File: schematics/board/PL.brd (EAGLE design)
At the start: 89 x 89 mm, 25 parts, among them IC2 STM32F103C8T, Q5 8MHz

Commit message: Исправлена плата TESTPL
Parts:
- added R1, R2, R3: 10k, resistor:R0603
- moved PWR 121.4 mm to (65.4, 41.8), turned to 180 degrees
- moved R102 112.5 mm to (54.7, 27.0), turned to 90 degrees
- moved R64 108.5 mm to (56.8, 49.5), turned to 270 degrees
- moved R79 107.7 mm to (43.0, 35.4), turned to 180 degrees
- moved C48 105.5 mm to (63.3, 40.2), turned to 270 degrees
- moved R101 104.4 mm to (52.6, 27.0), turned to 90 degrees
- moved U$23 102.3 mm to (55.5, 5.00)
- moved R27 101.3 mm to (54.6, 49.6), turned to 270 degrees
- moved C005R 97.1 mm to (46.0, 38.6)
- moved PB5 95.6 mm to (67.6, 41.8), turned to 180 degrees
- moved C44 92.6 mm to (26.5, 24.6), turned to 270 degrees
- moved R26 92.1 mm to (50.4, 49.5), turned to 270 degrees
- moved R82 92.1 mm to (65.4, 38.4), turned to 90 degrees
- moved MICS-6814 91.9 mm to (65.3, 67.7), turned to 180 degrees
- moved BME280 90.5 mm to (50.0, 69.0), turned to 180 degrees
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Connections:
- removed net VBAT: IC2.1
- new net SENS_CO: IC2.10, MICS-6814.P$5, R3.1
- new net SENS_NH3: IC2.11, MICS-6814.P$4, R2.1
- new net SENS_NO2: IC2.12, MICS-6814.P$3, R1.1
- new net SENS_O2: IC2.13, ME-O2.P$1
- net SCL: now also BME280.P$3
- net SDA: now also BME280.P$4
- net VDD: now also IC2.1, R1.2, R2.2, R3.2
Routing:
- net VDD: track 0.00 -> 140.4 mm, vias 0 -> 3
- net 5V: track 0.00 -> 109.7 mm
- net N$145: track 0.00 -> 6.50 mm
- net N$133: track 0.00 -> 6.41 mm
- net SENS_CO: track 0.00 -> 3.12 mm
- net SENS_NO2: track 0.00 -> 3.12 mm
- net SENS_NH3: track 0.00 -> 3.01 mm
- net N$159: track 0.00 -> 1.80 mm
- net N$1: track 0.00 -> 1.73 mm
- added copper zone on layer 1, net GND
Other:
- outline, holes or cut-outs redrawn

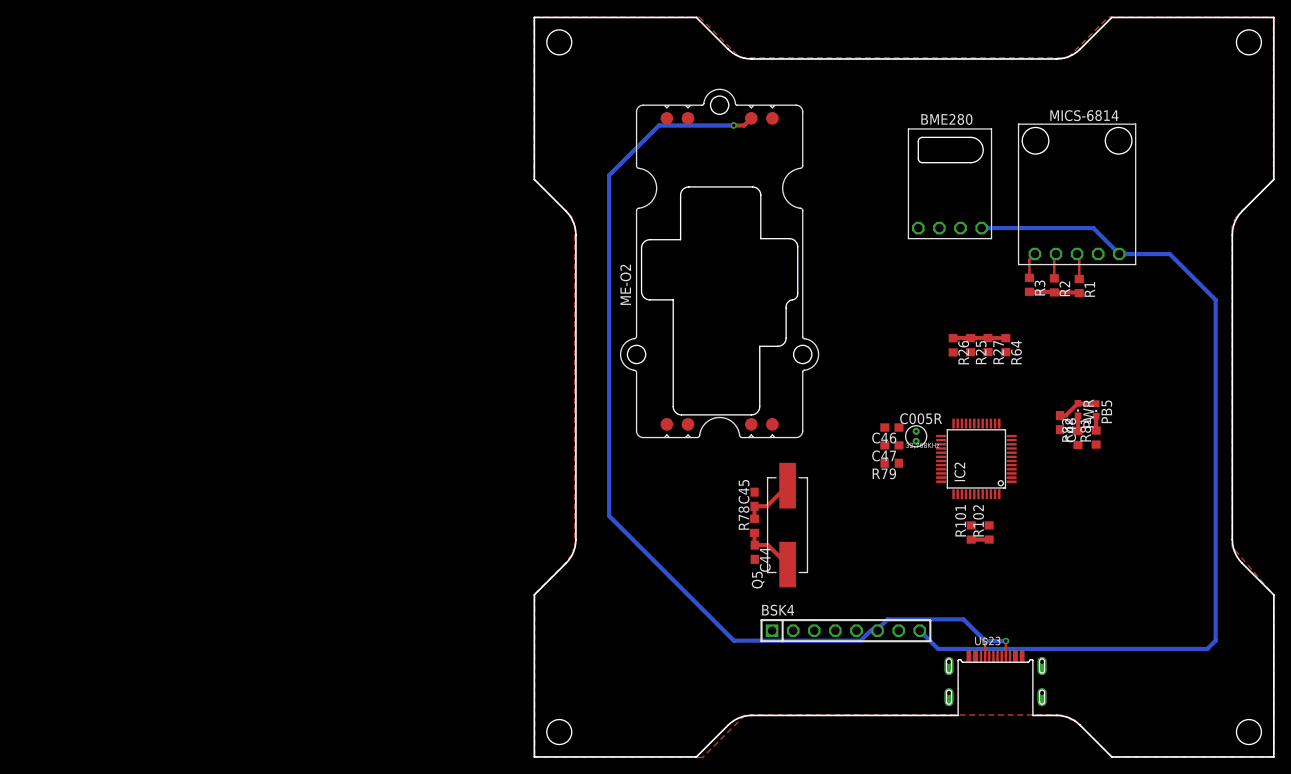
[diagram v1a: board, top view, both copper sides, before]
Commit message: Разведена плата PL
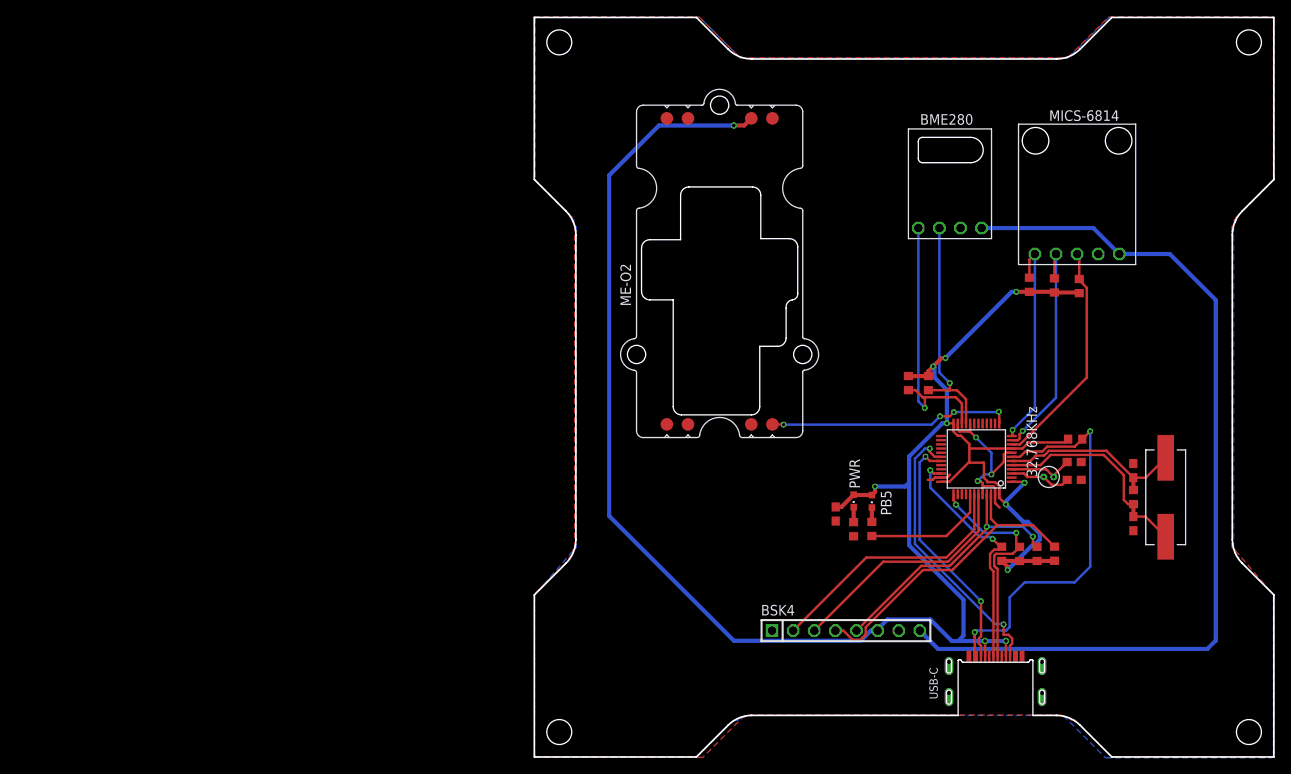
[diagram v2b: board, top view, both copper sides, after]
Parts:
- moved C44 46.6 mm to (72.1, 34.5), turned to 90 degrees
- moved R78 45.7 mm to (72.1, 31.3), turned to 270 degrees
- moved C45 45.7 mm to (72.1, 28.1), turned to 270 degrees
- moved Q5 45.6 mm to (76.0, 31.2), turned to 270 degrees
- moved PB5 29.2 mm to (40.6, 30.8)
- moved PWR 29.2 mm to (38.4, 30.8)
- moved R81 29.2 mm to (40.6, 27.4)
- moved C48 29.2 mm to (36.3, 29.2)
- moved R82 29.2 mm to (38.4, 27.4)
- moved R26 27.9 mm to (62.6, 24.5), turned to 90 degrees
- moved R25 26.4 mm to (60.5, 24.4), turned to 90 degrees
- moved R27 25.4 mm to (58.4, 24.4), turned to 90 degrees
- moved R64 25.1 mm to (56.2, 24.4), turned to 90 degrees
- moved C46 22.8 mm to (65.0, 33.4), turned to 0 degrees
- moved R79 22.3 mm to (65.1, 38.2), turned to 0 degrees
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- renumbered U$23 to USB-C
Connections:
- net SENS_CO: now also IC2.12; no longer IC2.10
- net SENS_NO2: now also IC2.10; no longer IC2.12
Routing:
- net VDD: track 140.4 -> 251.6 mm, vias 3 -> 11
- net NRST: track 0.00 -> 49.2 mm, vias 0 -> 2
- net SDATM: track 0.00 -> 38.2 mm
- net TX-C: track 0.00 -> 34.0 mm, vias 0 -> 2
- net SDA: track 0.00 -> 32.8 mm, vias 0 -> 1
- net SCLTM: track 0.00 -> 32.4 mm, vias 0 -> 2
- net TIME: track 0.00 -> 31.1 mm
- net RX-C: track 0.00 -> 29.7 mm, vias 0 -> 2
- net SWD: track 0.00 -> 29.4 mm, vias 0 -> 2
- net SENS_O2: track 0.00 -> 29.4 mm, vias 0 -> 4
- net I2CINT: track 0.00 -> 29.2 mm
- net SCL: track 0.00 -> 27.9 mm, vias 0 -> 1
- net SWC: track 0.00 -> 27.7 mm, vias 0 -> 2
- net SENS_NH3: track 3.01 -> 28.1 mm, vias 0 -> 1
- net GND: track 0.00 -> 24.9 mm, vias 0 -> 3
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- added copper zone on layer 16, net GND

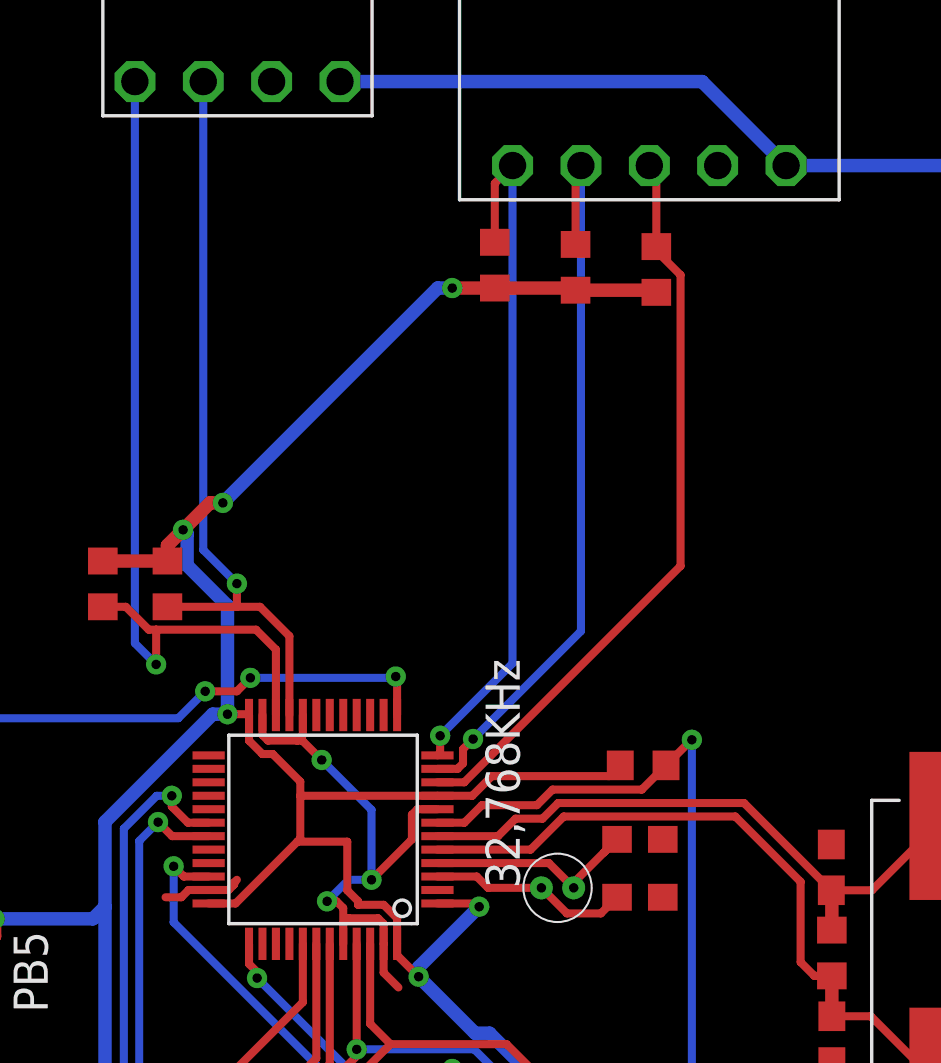
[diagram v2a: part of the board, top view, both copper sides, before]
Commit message: На плату полезной нагрузки добавлены управляемые резисторы для управления балансирующими сопротивлениями для газового датчика
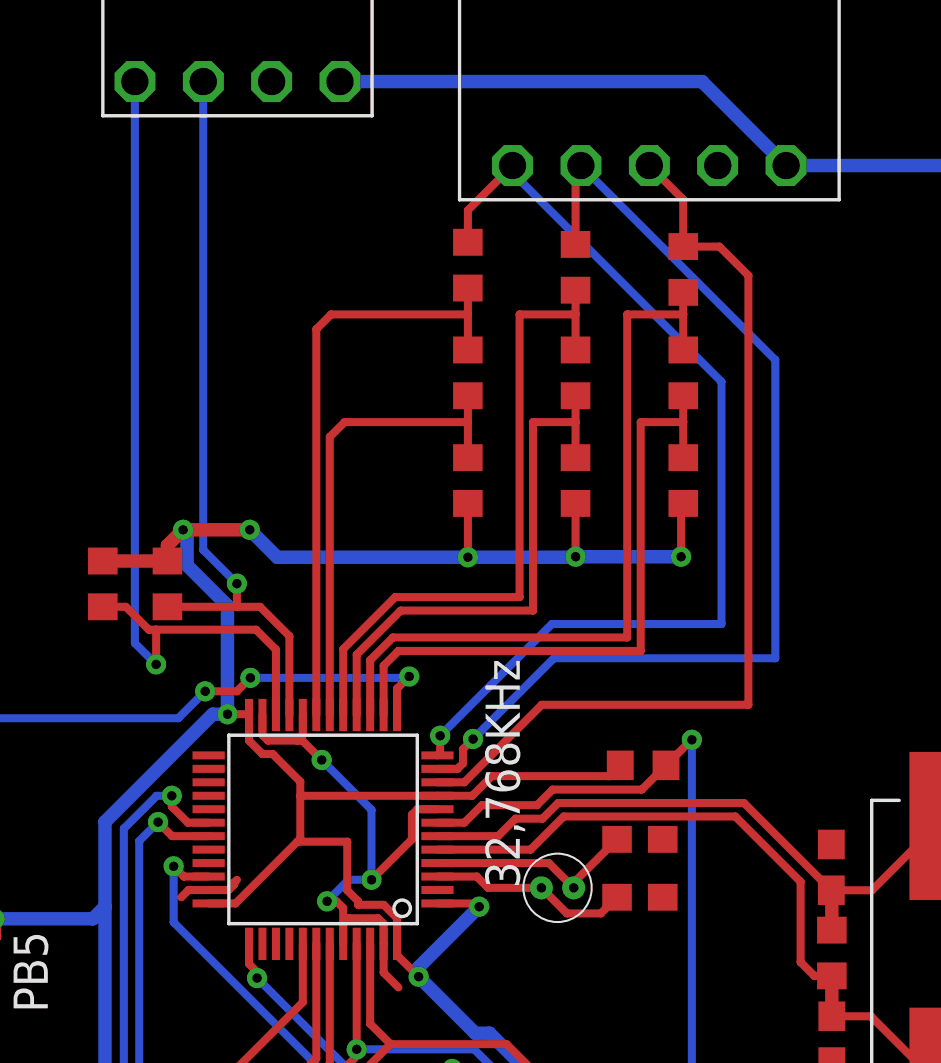
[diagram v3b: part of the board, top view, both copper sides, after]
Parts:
- added R4, R5, R6, R7, R8, R9: 10k, resistor:R0603
- moved R1 1.00 mm to (66.6, 56.7)
- moved R3 1.00 mm to (58.6, 56.8)
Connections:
- new net SENS_CTL_CO_1: IC2.19, R3.2, R6.1
- new net SENS_CTL_CO_2: IC2.18, R6.2, R7.1
- new net SENS_CTL_NH3_1: IC2.17, R2.2, R5.1
- new net SENS_CTL_NH3_2: IC2.16, R5.2, R8.1
- new net SENS_CTL_NO2_1: IC2.15, R1.2, R4.1
- new net SENS_CTL_NO2_2: IC2.14, R4.2, R9.1
- net VDD: now also R7.2, R8.2, R9.2; no longer R1.2, R2.2, R3.2
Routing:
- net SENS_CTL_NO2_1: track 0.00 -> 28.2 mm
- net SENS_CTL_NH3_1: track 0.00 -> 24.6 mm
- net SENS_CTL_NO2_2: track 0.00 -> 24.0 mm
- net SENS_CTL_CO_1: track 0.00 -> 22.5 mm
- net SENS_CTL_NH3_2: track 0.00 -> 20.4 mm
- net SENS_CTL_CO_2: track 0.00 -> 18.0 mm
- net SENS_NH3: track 28.1 -> 38.9 mm
- net SENS_CO: track 26.2 -> 36.7 mm
- net SENS_NO2: track 27.7 -> 35.1 mm
- net VDD: track 251.6 -> 255.2 mm, vias 11 -> 13
- net N$148: track 8.60 -> 7.91 mm
- net SENS_O2: track 29.4 -> 30.0 mm
- net GND: track 24.9 -> 24.3 mm

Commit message: Доработана плата БКУ
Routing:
- net SENS_NH3: track 38.9 -> 36.7 mm
- net SENS_NO2: track 35.1 -> 34.2 mm, vias 0 -> 2
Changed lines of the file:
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@@
 <?xml version="1.0" encoding="utf-8"?>
 <!DOCTYPE eagle SYSTEM "eagle.dtd">
-<eagle version="9.6.0">
+<eagle version="9.4.2">
 <drawing>
 <settings>
@@
 <vertex x="-0.05" y="69.55"/>
 </polygon>
-<wire x1="48.205025" y1="33.62" x2="47.935025" y2="33.35" width="0.3" layer="1"/>
 <wire x1="48.95" y1="33.62" x2="48.205025" y2="33.62" width="0.3" layer="1"/>
 <wire x1="55.45" y1="31.62" x2="55.45" y2="30.55" width="0.3" layer="1"/>
@@
 <wire x1="58.58" y1="58.87" x2="58.58" y2="57.68" width="0.3" layer="1"/>
 <contactref element="IC2" pad="12"/>
-<via x="57.55" y="39.35" extent="1-16" drill="0.35"/>
-<wire x1="57.55" y1="39.35" x2="57.55" y2="38.72" width="0.3" layer="1"/>
-<wire x1="57.55" y1="38.72" x2="57.45" y2="38.62" width="0.3" layer="1"/>
+<via x="58.05" y="39.35" extent="1-16" drill="0.35"/>
+<wire x1="58.05" y1="39.35" x2="58.05" y2="39.22" width="0.3" layer="1"/>
+<wire x1="58.05" y1="39.22" x2="57.45" y2="38.62" width="0.3" layer="1"/>
 <wire x1="61.7" y1="43.5" x2="68" y2="43.5" width="0.3" layer="16"/>
 <wire x1="68" y1="43.5" x2="68" y2="52.5" width="0.3" layer="16"/>
 <wire x1="60.24" y1="60.53" x2="60.24" y2="60.26" width="0.3" layer="16"/>
 <wire x1="68" y1="52.5" x2="60.24" y2="60.26" width="0.3" layer="16"/>
-<wire x1="57.55" y1="39.35" x2="61.7" y2="43.5" width="0.3" layer="16"/>
+<wire x1="61.7" y1="43.5" x2="58.05" y2="39.85" width="0.3" layer="16"/>
+<wire x1="58.05" y1="39.35" x2="58.05" y2="39.85" width="0.3" layer="16"/>
 </signal>
 <signal name="SENS_NH3">
@@
 <wire x1="62.78" y1="60.53" x2="62.58" y2="60.33" width="0.3" layer="1"/>
 <wire x1="62.58" y1="60.33" x2="62.58" y2="57.6" width="0.3" layer="1"/>
-<wire x1="58.772571875" y1="39.227428125" x2="61.772571875" y2="42.227428125" width="0.3" layer="16"/>
-<via x="58.772571875" y="39.227428125" extent="1-16" drill="0.35"/>
+<wire x1="59.272571875" y1="39.227428125" x2="59.272571875" y2="40.327428125" width="0.3" layer="16"/>
+<wire x1="61.922571875" y1="42.977428125" x2="59.272571875" y2="40.327428125" width="0.3" layer="16"/>
+<via x="59.272571875" y="39.227428125" extent="1-16" drill="0.35"/>
 <wire x1="58.194975" y1="38.12" x2="58.4" y2="38.325025" width="0.3" layer="1"/>
-<wire x1="58.4" y1="38.325025" x2="58.4" y2="38.85485625" width="0.3" layer="1"/>
-<wire x1="58.4" y1="38.85485625" x2="58.772571875" y2="39.227428125" width="0.3" layer="1"/>
+<wire x1="58.4" y1="38.325025" x2="58.4" y2="38.35485625" width="0.3" layer="1"/>
+<wire x1="58.4" y1="38.35485625" x2="59.272571875" y2="39.227428125" width="0.3" layer="1"/>
 <wire x1="57.45" y1="38.12" x2="58.194975" y2="38.12" width="0.3" layer="1"/>
-<wire x1="62.78" y1="60.53" x2="70" y2="53.31" width="0.3" layer="16"/>
-<wire x1="70" y1="53.31" x2="70" y2="42.227428125" width="0.3" layer="16"/>
-<wire x1="70" y1="42.227428125" x2="61.772571875" y2="42.227428125" width="0.3" layer="16"/>
+<wire x1="68.5" y1="52.81" x2="62.78" y2="58.53" width="0.3" layer="16"/>
+<wire x1="62.78" y1="60.53" x2="62.78" y2="58.53" width="0.3" layer="16"/>
+<wire x1="68.5" y1="52.81" x2="68.5" y2="42.977428125" width="0.3" layer="16"/>
+<wire x1="68.5" y1="42.977428125" x2="61.922571875" y2="42.977428125" width="0.3" layer="16"/>
 </signal>
 <signal name="SENS_NO2">
@@
 <wire x1="66.58" y1="59.27" x2="66.58" y2="57.52" width="0.3" layer="1"/>
 <contactref element="IC2" pad="10"/>
-<wire x1="57.45" y1="37.62" x2="58.444975" y2="37.62" width="0.3" layer="1"/>
-<wire x1="66.58" y1="57.52" x2="67.924975" y2="57.52" width="0.3" layer="1"/>
-<wire x1="69" y1="56.444975" x2="67.924975" y2="57.52" width="0.3" layer="1"/>
-<wire x1="69" y1="40.5" x2="69" y2="56.444975" width="0.3" layer="1"/>
-<wire x1="58.444975" y1="37.62" x2="61.324975" y2="40.5" width="0.3" layer="1"/>
-<wire x1="69" y1="40.5" x2="61.324975" y2="40.5" width="0.3" layer="1"/>
+<via x="67.87" y="56.625025" extent="1-16" drill="0.35"/>
+<wire x1="66.58" y1="57.52" x2="66.975025" y2="57.52" width="0.3" layer="1"/>
+<wire x1="66.975025" y1="57.52" x2="67.87" y2="56.625025" width="0.3" layer="1"/>
+<wire x1="67.87" y1="56.625025" x2="67.87" y2="54.1471125" width="0.3" layer="16"/>
+<wire x1="69" y1="53.0171125" x2="69" y2="42.5" width="0.3" layer="16"/>
+<wire x1="69" y1="42.5" x2="68.729684375" y2="42.5" width="0.3" layer="16"/>
+<wire x1="68.729684375" y1="42.5" x2="68.7071125" y2="42.477428125" width="0.3" layer="16"/>
+<wire x1="62.5" y1="42.477428125" x2="68.7071125" y2="42.477428125" width="0.3" layer="16"/>
+<wire x1="67.87" y1="54.1471125" x2="69" y2="53.0171125" width="0.3" layer="16"/>
+<via x="60" y="38.5782" extent="1-16" drill="0.35"/>
+<wire x1="58.535775" y1="37.62" x2="59.265775" y2="38.35" width="0.3" layer="1"/>
+<wire x1="59.265775" y1="38.35" x2="59.7718" y2="38.35" width="0.3" layer="1"/>
+<wire x1="59.7718" y1="38.35" x2="60" y2="38.5782" width="0.3" layer="1"/>
+<wire x1="60.000771875" y1="39.9782" x2="60.000771875" y2="38.578971875" width="0.3" layer="16"/>
+<wire x1="60" y1="38.5782" x2="60.000771875" y2="38.578971875" width="0.3" layer="16"/>
+<wire x1="60.000771875" y1="39.9782" x2="62.5" y2="42.477428125" width="0.3" layer="16"/>
+<wire x1="57.45" y1="37.62" x2="58.535775" y2="37.62" width="0.3" layer="1"/>
 </signal>
 <signal name="SENS_O2">
@@
 <contactref element="IC2" pad="15"/>
 <wire x1="66.58" y1="55" x2="66.58" y2="53.68" width="0.3" layer="1"/>
-<wire x1="54.95" y1="42.1571125" x2="55.7928875" y2="43" width="0.3" layer="1"/>
+<wire x1="54.95" y1="42.1571125" x2="56.2928875" y2="43.5" width="0.3" layer="1"/>
 <wire x1="54.95" y1="40.12" x2="54.95" y2="42.1571125" width="0.3" layer="1"/>
-<wire x1="64.5" y1="43" x2="64.5" y2="55" width="0.3" layer="1"/>
+<wire x1="64.5" y1="43.5" x2="64.5" y2="55" width="0.3" layer="1"/>
 <wire x1="64.5" y1="55" x2="66.58" y2="55" width="0.3" layer="1"/>
-<wire x1="55.7928875" y1="43" x2="64.5" y2="43" width="0.3" layer="1"/>
+<wire x1="56.2928875" y1="43.5" x2="64.5" y2="43.5" width="0.3" layer="1"/>
 </signal>
 <signal name="SENS_CTL_NO2_2">
@@
 <wire x1="66.58" y1="51" x2="66.58" y2="49.68" width="0.3" layer="1"/>
 <wire x1="55.45" y1="40.12" x2="55.45" y2="41.95" width="0.3" layer="1"/>
-<wire x1="56" y1="42.5" x2="65" y2="42.5" width="0.3" layer="1"/>
-<wire x1="65" y1="42.5" x2="65" y2="51" width="0.3" layer="1"/>
+<wire x1="56.5" y1="43" x2="65" y2="43" width="0.3" layer="1"/>
+<wire x1="65" y1="43" x2="65" y2="51" width="0.3" layer="1"/>
 <wire x1="65" y1="51" x2="66.58" y2="51" width="0.3" layer="1"/>
-<wire x1="55.45" y1="41.95" x2="56" y2="42.5" width="0.3" layer="1"/>
+<wire x1="55.45" y1="41.95" x2="56.5" y2="43" width="0.3" layer="1"/>
 </signal>
 </signals>

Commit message: Изменения в подключении мк
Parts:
- added C15, C53, C54, C55: 100nF, rcl:C0603
- added C16: 10µ, rcl:C1206
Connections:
- net GND: now also C15.2, C16.2, C53.2, C54.2, C55.2
- net VDD: now also C15.1, C16.1, C53.1, C54.1, C55.1
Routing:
- net GND: track 23.9 -> 40.0 mm
- net VDD: track 255.2 -> 262.9 mm
- net SENS_O2: track 30.0 -> 30.6 mm
- net SDA: track 32.8 -> 32.3 mm

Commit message: Обновлены герберы плат
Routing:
- net VDD: track 262.9 -> 265.3 mm
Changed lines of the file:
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@@
 <param name="mvStopFrame" value="1"/>
 <param name="mvCreamFrame" value="0"/>
-<param name="mlMinStopFrame" value="4mil"/>
-<param name="mlMaxStopFrame" value="4mil"/>
+<param name="mlMinStopFrame" value="2mil"/>
+<param name="mlMaxStopFrame" value="2mil"/>
 <param name="mlMinCreamFrame" value="0mil"/>
 <param name="mlMaxCreamFrame" value="0mil"/>
@@
 <wire x1="55.95" y1="32.5720875" x2="55.95" y2="31.62" width="0.3" layer="1"/>
 <wire x1="48.95" y1="33.12" x2="49.95" y2="33.12" width="0.3" layer="1"/>
-<wire x1="64.24" y1="38.25" x2="62.64" y2="39.85" width="0.3" layer="1"/>
 <via x="49.65" y="40.15" extent="1-16" drill="0.35"/>
-<wire x1="62" y1="39.85" x2="62.64" y2="39.85" width="0.3" layer="1"/>
 <wire x1="45.1" y1="25.47966875" x2="51.6532" y2="18.92646875" width="0.5" layer="16"/>
 <wire x1="45.1" y1="25.47966875" x2="45.1" y2="33" width="0.5" layer="16"/>
@@
 <wire x1="57.15" y1="30.6" x2="57" y2="30.6" width="0.3" layer="1"/>
 <wire x1="60.60163125" y1="37.85" x2="61.1282" y2="38.37656875" width="0.3" layer="1"/>
-<wire x1="61.1282" y1="38.37656875" x2="61.1282" y2="38.9782" width="0.3" layer="1"/>
-<wire x1="61.1282" y1="38.9782" x2="62" y2="39.85" width="0.3" layer="1"/>
 <wire x1="59.035775" y1="37.12" x2="59.765775" y2="37.85" width="0.3" layer="1"/>
 <wire x1="59.765775" y1="37.85" x2="60.60163125" y2="37.85" width="0.3" layer="1"/>
 <wire x1="57.45" y1="37.12" x2="59.035775" y2="37.12" width="0.3" layer="1"/>
-<wire x1="62" y1="39.85" x2="62" y2="39.95" width="0" layer="19" extent="1-1"/>
-<wire x1="47.4" y1="30.75" x2="46.45" y2="32.6" width="0" layer="19" extent="1-1"/>
+<wire x1="61.1282" y1="39.0782" x2="62" y2="39.95" width="0.3" layer="1"/>
+<wire x1="61.1282" y1="38.37656875" x2="61.1282" y2="39.0782" width="0.3" layer="1"/>
+<wire x1="62" y1="39.95" x2="62.54" y2="39.95" width="0.3" layer="1"/>
+<wire x1="62.54" y1="39.95" x2="64.24" y2="38.25" width="0.3" layer="1"/>
+<wire x1="46.45" y1="32.6" x2="46.45" y2="31.7" width="0.3" layer="1"/>
+<wire x1="46.45" y1="31.7" x2="47.4" y2="30.75" width="0.3" layer="1"/>
 </signal>
 <signal name="N$133">
